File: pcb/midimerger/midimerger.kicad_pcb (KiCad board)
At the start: 2 copper layers, 71.1 x 69.8 mm, 11 parts, among them J1 USB_A, J2 MIDI_1_IN, J3 MIDI_1_OUT, U1 Teensy3.6, U2 6N138

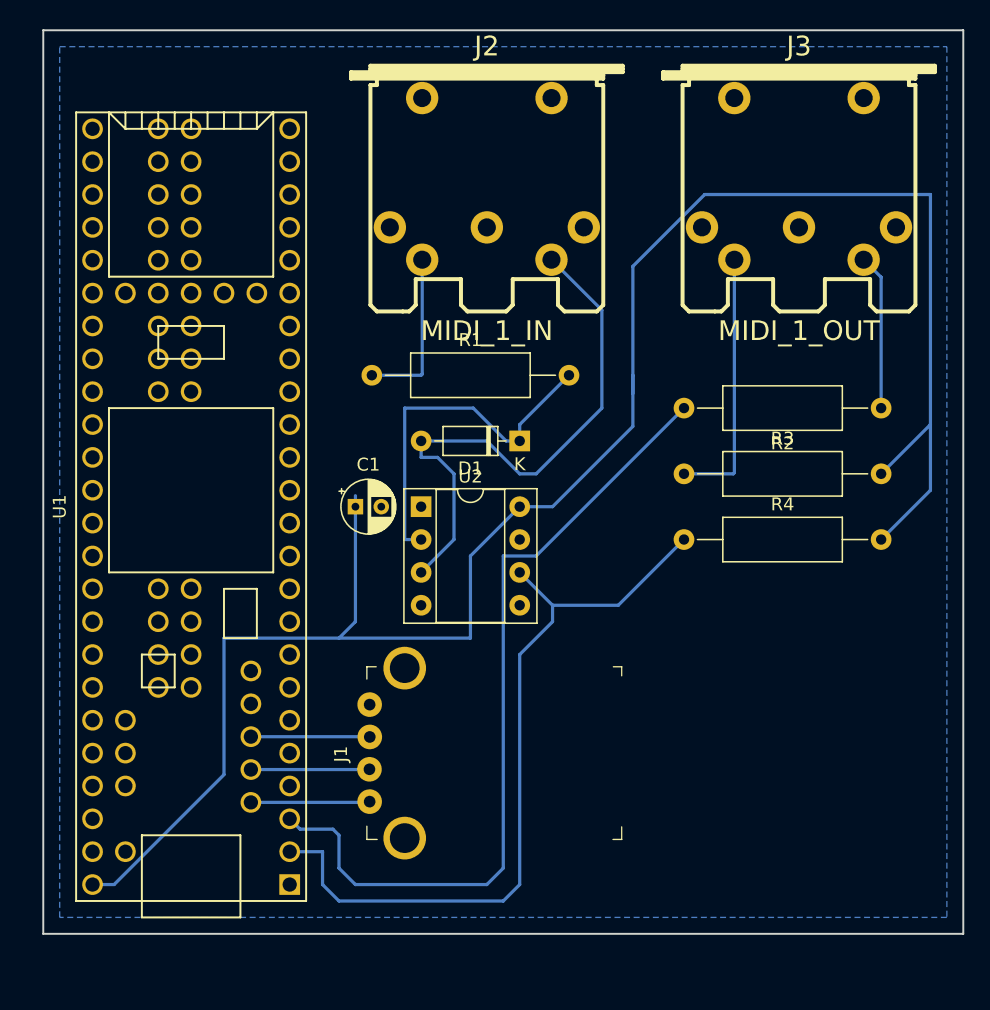
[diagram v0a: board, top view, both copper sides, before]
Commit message: made trace thicker
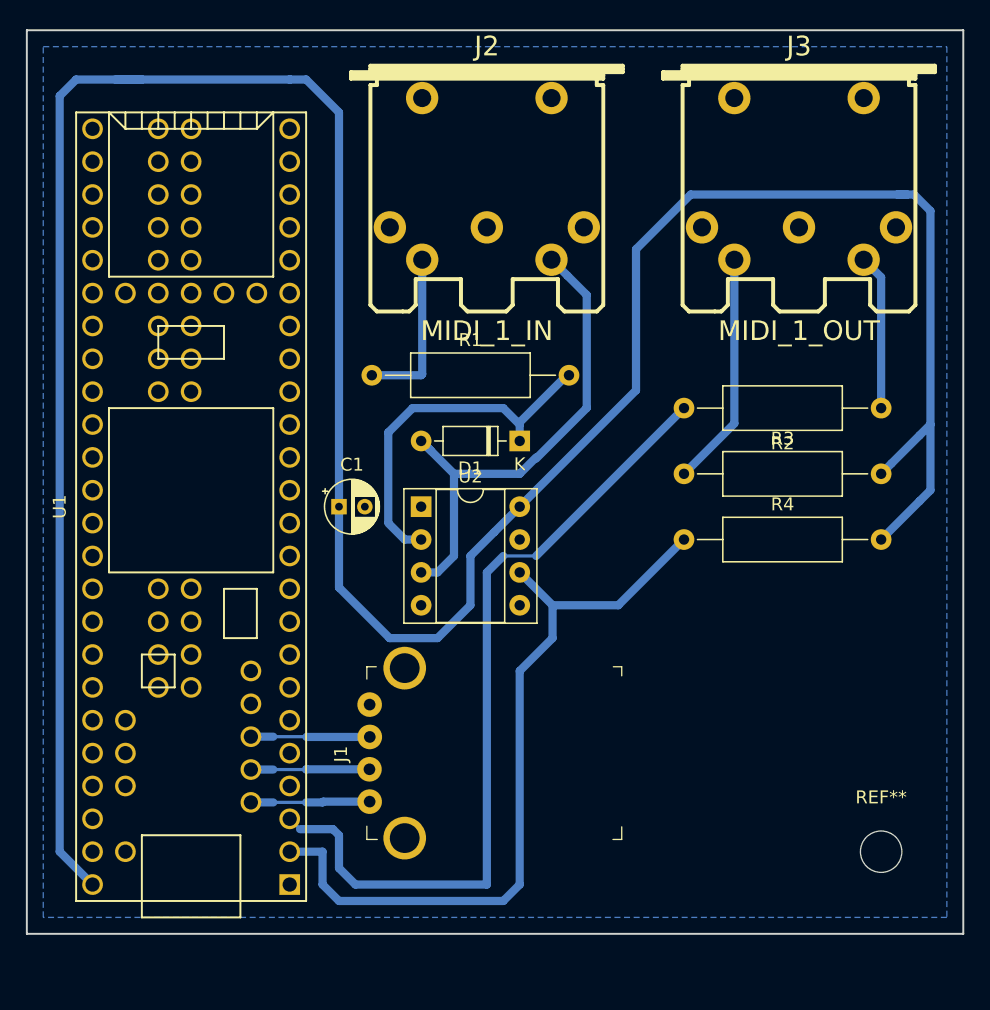
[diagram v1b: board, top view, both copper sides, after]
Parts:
- added REF**: MountingHole_3.2mm_M3, MountingHole:MountingHole_3.2mm_M3, F.Cu at (167.6, 104.1)
- moved C1 1.27 mm to (125.7, 77.5)
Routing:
- net /5V: track 150.6 -> 227.8 mm
- net /H_USB_D+: track 9.20 -> 15.9 mm
- net Net-(D1-Pad2): track 43.2 -> 39.2 mm
- net Net-(J3-Pad4): track 20.4 -> 18.2 mm
- net /H_USB_D-: track 9.17 -> 10.9 mm
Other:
- board size 71.1 x 69.8 mm -> 72.4 x 69.8 mm
- net class Default: clearance 0.2 -> 0.254
- rule trace_clearance: 0.2 -> 0.254

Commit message: added export
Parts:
- added REF**: MountingHole_3.2mm_M3, MountingHole:MountingHole_3.2mm_M3, F.Cu at (114.3, 76.2)
- R1, R2, R3, R4: footprint Resistor_THT:R_Axial_DIN0309_L9.0mm_D3.2mm_P15.24mm_Horizontal -> Resistor_THT:R_Axial_DIN0309_L9.0mm_D3.2mm_P12.70mm_Horizontal
- moved R2 2.54 mm to (165.1, 69.8)
- moved REF** 1.27 mm to (166.4, 104.1)
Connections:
- J1 pad 4: GND -> Net-(J1-Pad4)
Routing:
- net /5V: track 227.8 -> 232.4 mm
- net Net-(J2-Pad4): track 12.8 -> 10.5 mm
- net Net-(D1-Pad1): track 28.2 -> 27.2 mm

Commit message: updated pcb
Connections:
- J1 pad 4: Net-(J1-Pad4) -> GND

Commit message: increased teensy pad size
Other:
- rule trace_min: 0.2 -> 0.01

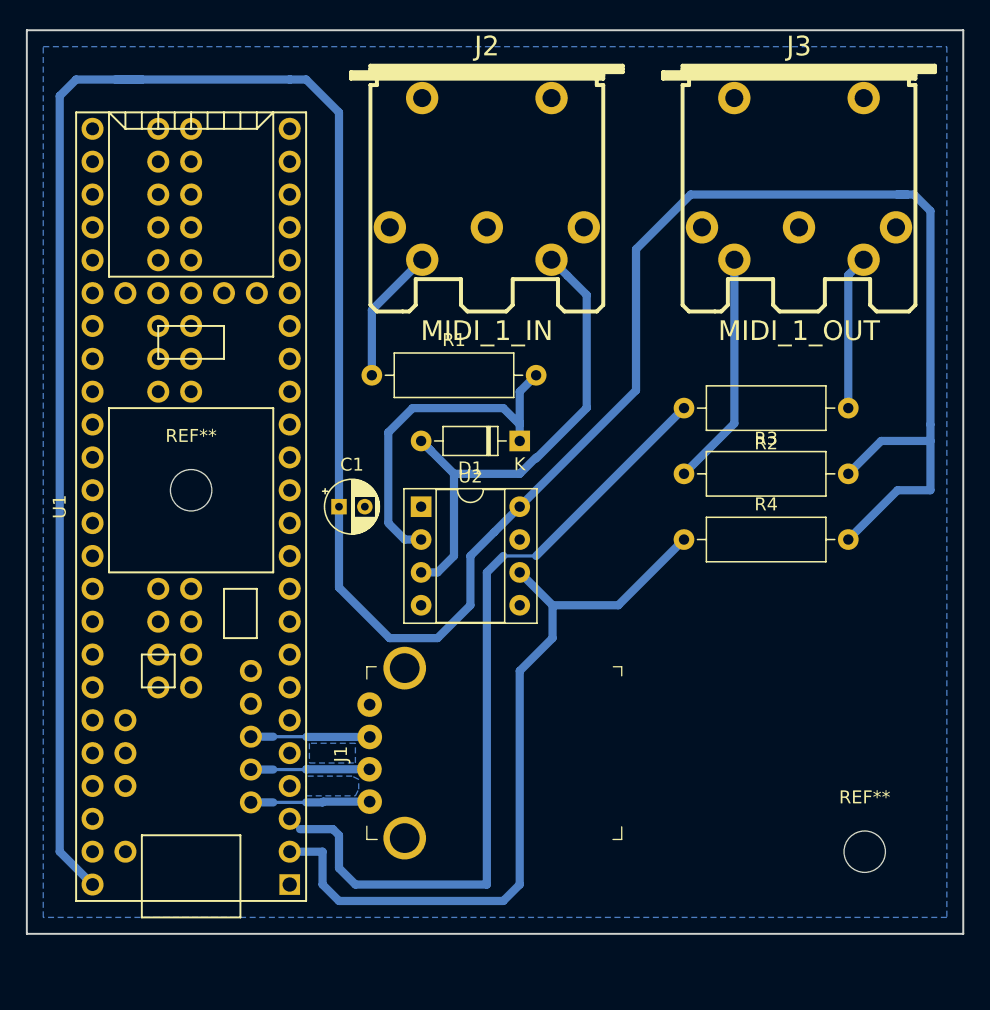
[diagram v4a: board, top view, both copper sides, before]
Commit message: fixed pcb ground and pull up voltage
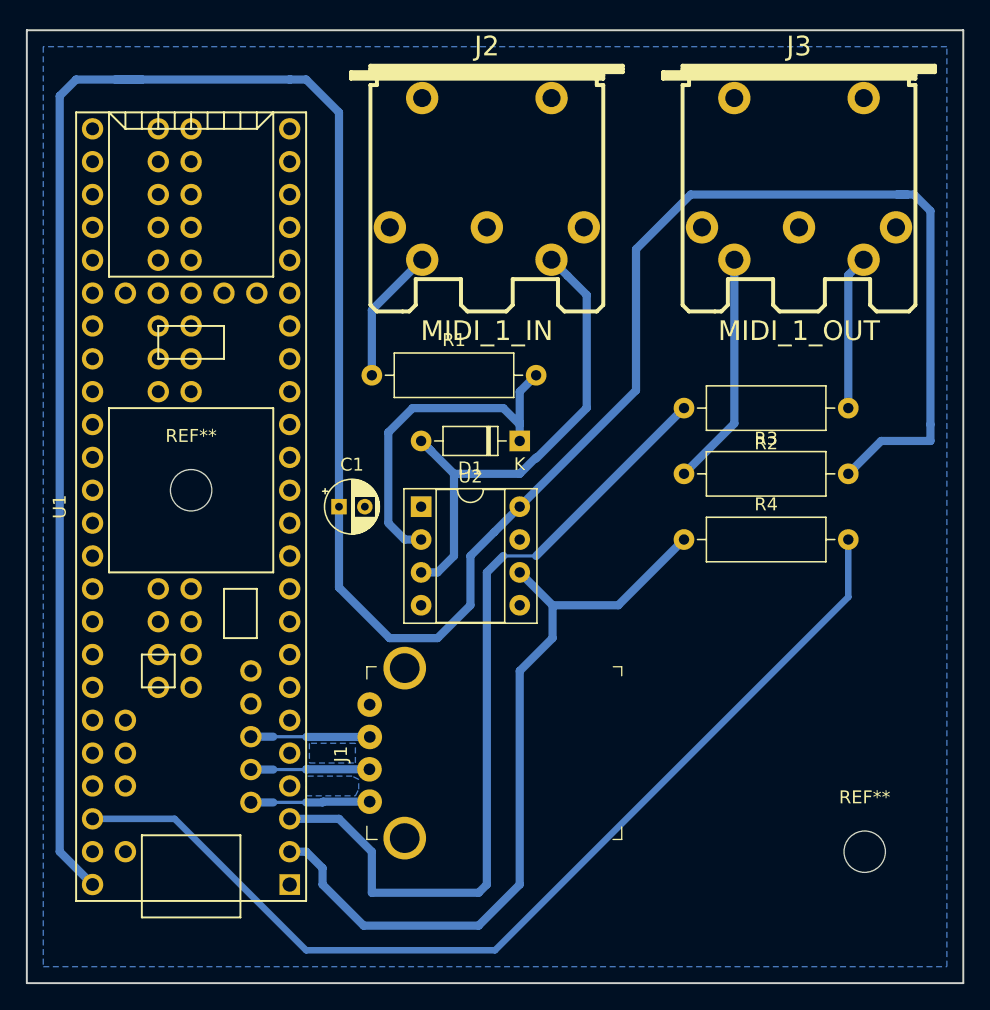
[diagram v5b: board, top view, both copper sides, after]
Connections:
- C1 pad 1: /5V -> Net-(C1-Pad1)
- R4 pad 2: /5V -> /3.3V
- U1 pad 51: Net-(U1-Pad51) -> /3.3V
- U2 pad 8: /5V -> Net-(C1-Pad1)
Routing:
- net /3.3V: track 0.00 -> 78.4 mm
- net /5V: track 232.4 -> 220.6 mm
- net /MIDI_1_OUT: track 63.5 -> 64.4 mm
- net /MIDI_1_IN: track 59.9 -> 60.7 mm
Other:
- board size 72.4 x 69.8 mm -> 72.4 x 73.7 mm
- net class Default: clearance 0.254 -> 0.1016; trace_width 0.25 -> 0.1524; via_dia 0.8 -> 0.599999; via_drill 0.4 -> 0.299999
- rule trace_clearance: 0.254 -> 0.1016
- rule trace_min: 0.01 -> 0.0889
- rule via_min_drill: 0.3 -> 0.299999
- rule via_min_size: 0.4 -> 0.599999
